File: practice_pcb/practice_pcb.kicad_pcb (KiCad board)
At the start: 2 copper layers, 61.5 x 44 mm, 22 parts, among them J1 VEE connector, J2 From_MCU, J3 MOSFET_out, J4 Conn_01x03, J5 Conn_01x01_Socket, J6 Conn_01x01_Socket, Q4 IRF3710, U1 LDO-3.3, U5 NSi6651A

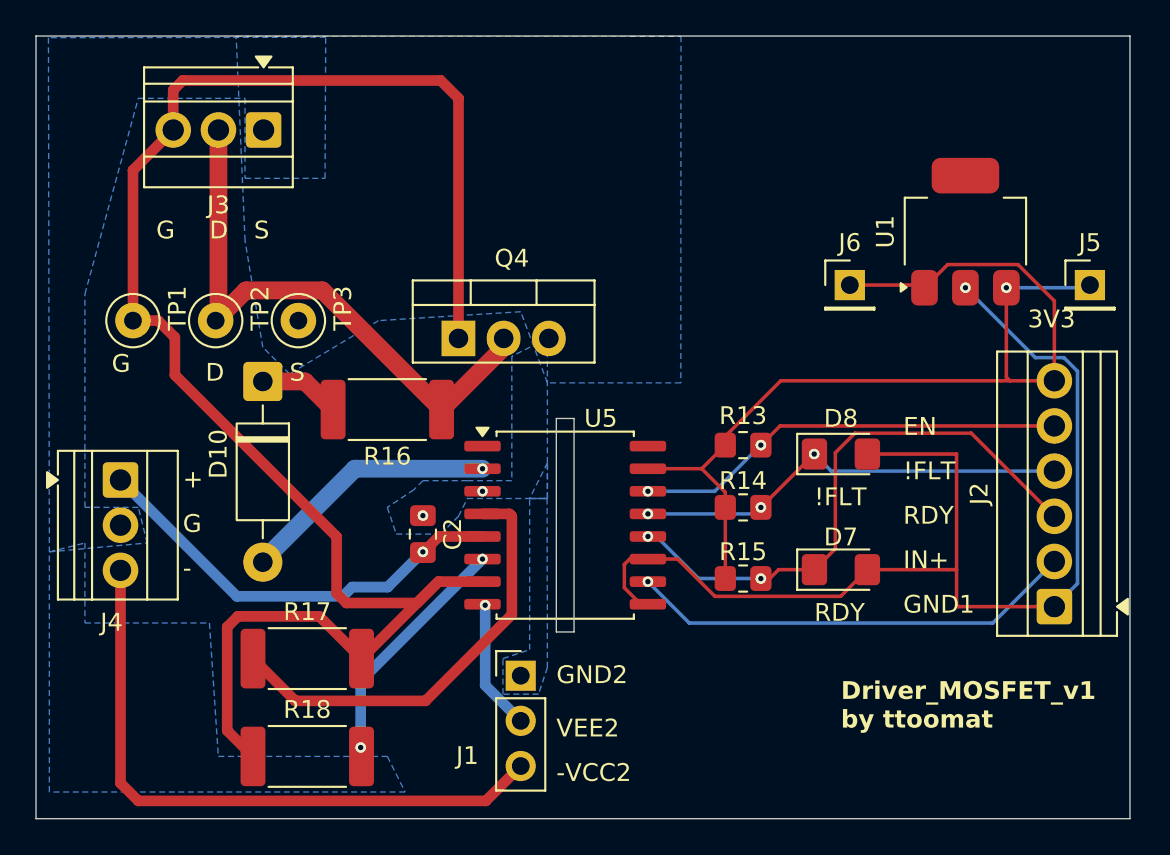
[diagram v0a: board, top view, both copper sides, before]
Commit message: practice_pcb driver schematics changed (leds).
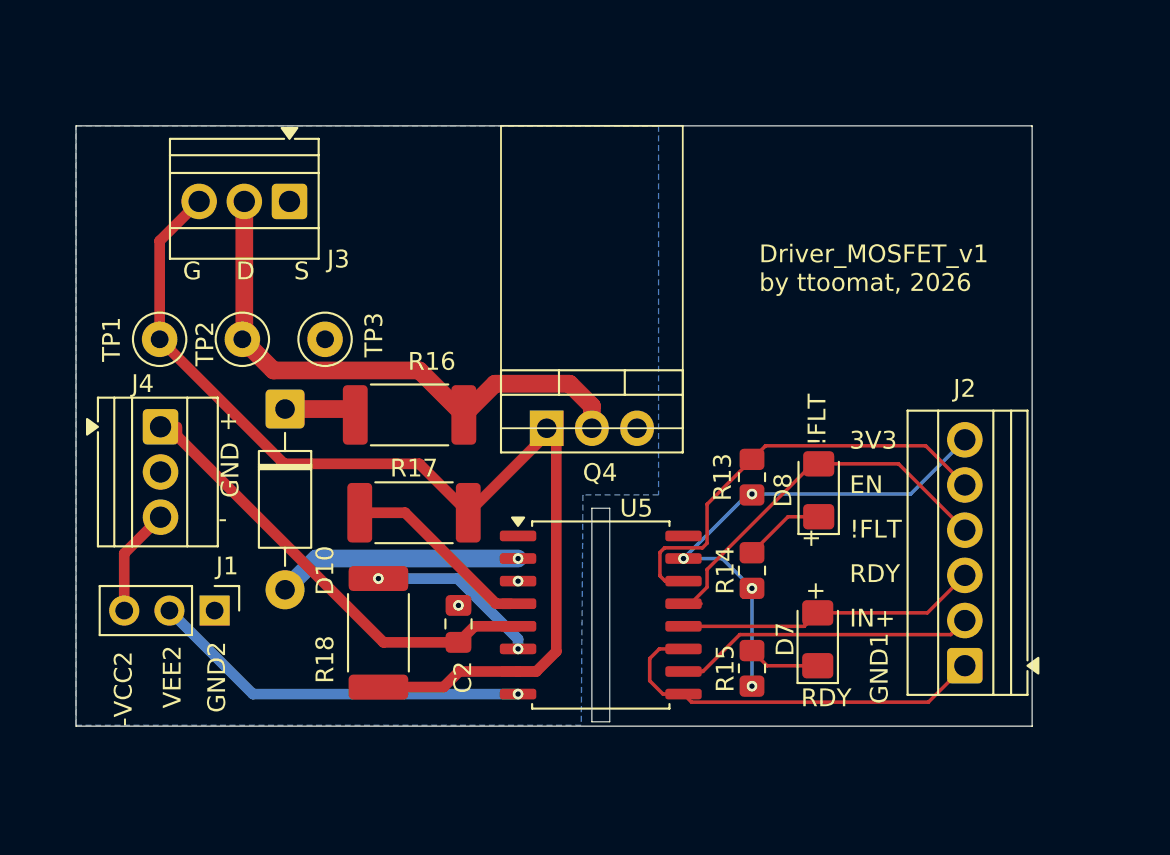
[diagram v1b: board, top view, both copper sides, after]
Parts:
- removed J5, J6: Conn_01x01_Socket, Connector_PinHeader_2.54mm:PinHeader_1x01_P2.54mm_Vertical
- removed U1: LDO-3.3, Package_TO_SOT_SMD:SOT-223-3_TabPin2
- R13, R14, R15: value 4.7k -> 1k
- moved J1 17.6 mm to (93.8, 84.8), turned to -90 degrees
- moved R17 10.2 mm to (105.0, 79.3)
- moved R18 8.02 mm to (103.0, 86.0), turned to 90 degrees
- moved Q4 7.08 mm to (112.5, 74.5)
- moved J2 6.03 mm to (136.0, 87.9)
- moved C2 5.43 mm to (107.5, 85.5)
- moved U5 5.43 mm to (115.5, 85.0)
- moved R15 5.07 mm to (124.0, 88.0), turned to 90 degrees
- moved J3 4.27 mm to (98.0, 61.8)
- moved D7 4.13 mm to (127.7, 86.4), turned to 90 degrees
- moved J4 3.74 mm to (90.8, 74.5)
- moved R14 3.59 mm to (124.0, 82.5), turned to 90 degrees
- moved D8 2.39 mm to (127.8, 78.0), turned to 90 degrees
- moved D10 1.99 mm to (97.8, 73.5)
- moved R13 1.87 mm to (124.0, 77.3), turned to 90 degrees
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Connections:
- D7 pad 2: GND_DRV1 -> Net-(D7-A)
- D8 pad 2: GND_DRV1 -> Net-(D8-A)
- J2 pad 3: Net-(D7-K) -> Net-(D7-A)
- J2 pad 4: Net-(D8-K) -> Net-(D8-A)
- J2 pad 6: Net-(J2-Pin_6) -> +3V3_DRV1
- U5 pad 12: Net-(D7-K) -> Net-(D7-A)
- U5 pad 13: Net-(D8-K) -> Net-(D8-A)
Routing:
- net GND_DRV1: track 64.4 -> 22.8 mm, vias 1 -> 0
- net Net-(J3-Pin_3): track 96.7 -> 61.5 mm
- net -15_DRV2: track 35.7 -> 6.09 mm
- net Net-(D7-K): track 32.3 -> 4.05 mm, vias 2 -> 0
- net Net-(D8-A): track 0.00 -> 22.2 mm
- net Net-(D8-K): track 24.7 -> 4.59 mm, vias 3 -> 0
- net Net-(J2-Pin_6): track 17.0 -> 0.00 mm
- net Net-(D7-A): track 0.00 -> 17.0 mm
- net Net-(J1-Pin_2): track 7.33 -> 21.5 mm
- net Net-(U5-OUTH): track 24.8 -> 11.0 mm
- net +3V3_DRV1: track 42.2 -> 29.6 mm, vias 1 -> 4
- net Net-(J2-Pin_2): track 25.2 -> 17.1 mm, vias 1 -> 0
- net Net-(U5-OUTL): track 13.4 -> 9.81 mm
- net +15_DRV2: track 24.5 -> 25.8 mm, vias 1 -> 0
- net /SINE (from OpAmp): track 32.6 -> 31.7 mm
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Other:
- board size 61.5 x 44 mm -> 53.8 x 33.8 mm
- board text added: "Driver_MOSFET_v1 by ttoomat, 2026"
- board text added: "GND"
- board text removed: "Driver_MOSFET_v1 by ttoomat"

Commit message: Driver board: castellated holes. SMD diode.
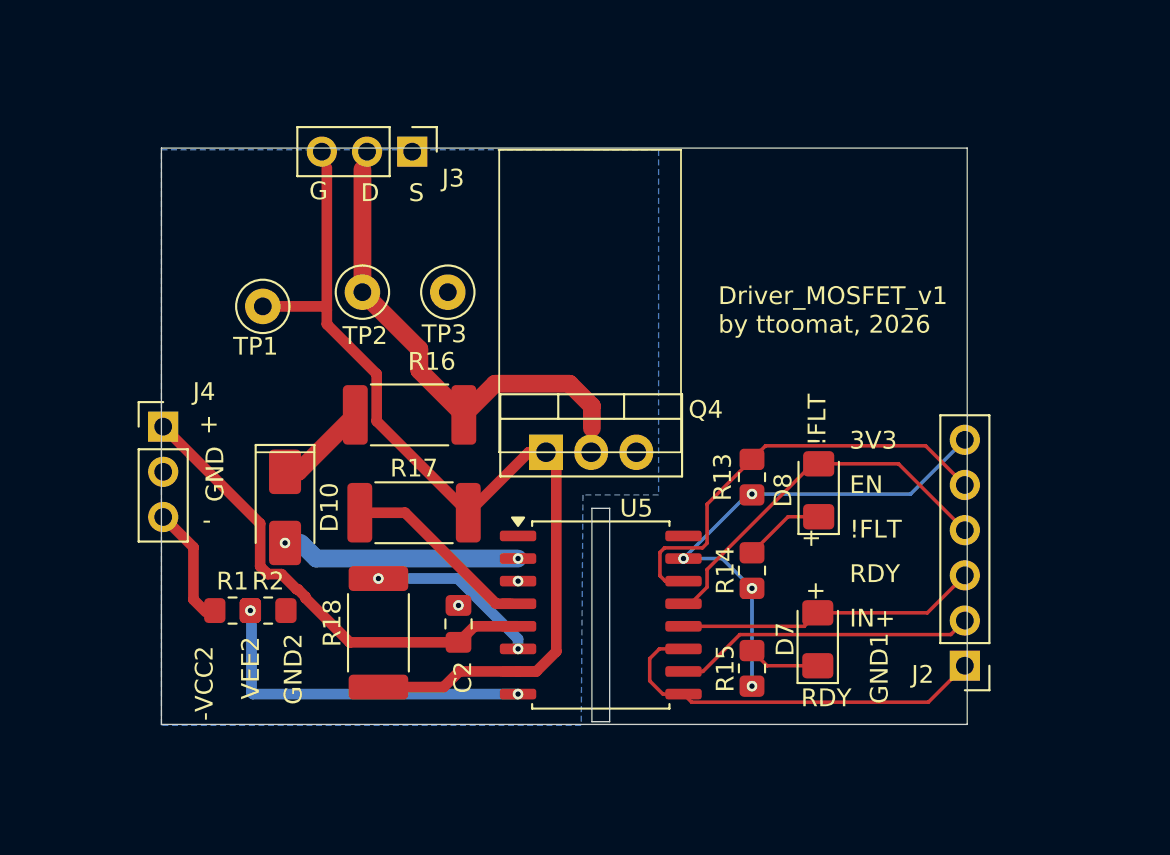
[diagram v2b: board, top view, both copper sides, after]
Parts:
- removed J1: VEE connector, Connector_PinHeader_2.54mm:PinHeader_1x03_P2.54mm_Vertical
- added R1: 0, Resistor_SMD:R_0805_2012Metric_Pad1.20x1.40mm_HandSolder, F.Cu at (94.8, 84.8)
- added R2: 0, Resistor_SMD:R_0805_2012Metric_Pad1.20x1.40mm_HandSolder, F.Cu at (96.8, 84.8)
- D10: value 1N4006 -> S1K-13-F; footprint Diode_THT:D_DO-41_SOD81_P10.16mm_Horizontal -> Diode_SMD:D_SMA
- J2: footprint TerminalBlock:TerminalBlock_Xinya_XY308-2.54-6P_1x06_P2.54mm_Horizontal -> Connector_PinHeader_2.54mm:PinHeader_1x06_P2.54mm_Vertical
- J3, J4: footprint TerminalBlock:TerminalBlock_Xinya_XY308-2.54-3P_1x03_P2.54mm_Horizontal -> Connector_PinHeader_2.54mm:PinHeader_1x03_P2.54mm_Vertical
- moved J3 7.45 mm to (104.9, 59.0), turned to -90 degrees
- moved TP3 7.39 mm to (106.9, 66.9)
- moved TP2 7.25 mm to (102.1, 66.9)
- moved TP1 6.09 mm to (96.5, 67.7)
- moved D10 5.53 mm to (97.8, 79.0)
- moved Q4 1.35 mm to (112.4, 75.9)
- moved J4 0.15 mm to (90.9, 74.5), turned to 0 degrees
- turned J2 to 180 degrees
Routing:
- net Net-(J3-Pin_3): track 61.5 -> 55.2 mm
- net /SINE (from OpAmp): track 31.7 -> 25.9 mm
- net Net-(R1-Pad2): track 21.5 -> 19.5 mm, vias 1 -> 2
- net Net-(D10-K): track 4.09 -> 5.74 mm
- net Net-(D8-A): track 22.2 -> 21.2 mm
- net Net-(D10-A): track 13.8 -> 13.5 mm, vias 1 -> 2
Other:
- board size 53.8 x 33.8 mm -> 45.3 x 32.4 mm

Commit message: Driver PCB leds error fixed.
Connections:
- D7 pad 2: Net-(D7-A) -> GND_DRV1
- D8 pad 2: Net-(D8-A) -> GND_DRV1
- J2 pad 3: Net-(D7-A) -> Net-(D7-K)
- J2 pad 4: Net-(D8-A) -> Net-(D8-K)
- U5 pad 12: Net-(D7-A) -> Net-(D7-K)
- U5 pad 13: Net-(D8-A) -> Net-(D8-K)
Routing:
- net GND_DRV1: track 22.8 -> 52.2 mm
- net Net-(D8-A): track 21.2 -> 0.00 mm
- net Net-(D7-A): track 17.0 -> 0.00 mm
- net Net-(D7-K): track 4.05 -> 18.8 mm, vias 0 -> 1
- net Net-(D8-K): track 4.59 -> 17.7 mm
- net Net-(J2-Pin_2): track 17.1 -> 18.3 mm, vias 0 -> 1
- net Net-(J2-Pin_5): track 25.2 -> 24.6 mm
- net GND_DRV2: vias 2 -> 3
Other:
- board size 45.3 x 32.4 mm -> 45.4 x 32.4 mm

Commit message: Lab consultation.
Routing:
- net /SINE (from OpAmp): track 25.9 -> 28.3 mm
- net Net-(J3-Pin_3): track 55.2 -> 56.2 mm
- net Net-(D10-A): track 13.5 -> 14.3 mm
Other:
- board size 45.4 x 32.4 mm -> 49 x 34.2 mm
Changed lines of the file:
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@@
 	)
 	(gr_rect
-		(start 90.8 58.8)
-		(end 136.2 91.2)
+		(start 89 57)
+		(end 138 91.2)
 		(stroke
 			(width 0.05)
@@
 	)
 	(segment
+		(start 120.855 90.2)
+		(end 120.15 89.495)
+		(width 0.2)
+		(layer "F.Cu")
+		(net "GND_DRV1")
+	)
+	(segment
+		(start 137.1175 86.75)
+		(end 137.1175 79.803654)
+		(width 0.2)
+		(layer "F.Cu")
+		(net "GND_DRV1")
+	)
+	(segment
+		(start 120.545552 86.955)
+		(end 120.15 86.955)
+		(width 0.2)
+		(layer "F.Cu")
+		(net "GND_DRV1")
+	)
+	(segment
+		(start 118.25 87.5)
+		(end 118.25 88.75)
+		(width 0.2)
+		(layer "F.Cu")
+		(net "GND_DRV1")
+	)
+	(segment
+		(start 135.9675 87.9)
+		(end 137.1175 86.75)
+		(width 0.2)
+		(layer "F.Cu")
+		(net "GND_DRV1")
+	)
+	(segment
+		(start 130.325 79.125)
+		(end 127.75 76.55)
+		(width 0.2)
+		(layer "F.Cu")
+		(net "GND_DRV1")
+	)
+	(segment
+		(start 133.6675 90.2)
+		(end 120.855 90.2)
+		(width 0.2)
+		(layer "F.Cu")
+		(net "GND_DRV1")
+	)
+	(segment
+		(start 118.795 86.955)
+		(end 118.25 87.5)
+		(width 0.2)
+		(layer "F.Cu")
+		(net "GND_DRV1")
+	)
+	(segment
+		(start 136.438846 79.125)
+		(end 130.325 79.125)
+		(width 0.2)
+		(layer "F.Cu")
+		(net "GND_DRV1")
+	)
+	(segment
+		(start 118.995 89.495)
+		(end 120.15 89.495)
+		(width 0.2)
+		(layer "F.Cu")
+		(net "GND_DRV1")
+	)
+	(segment
+		(start 137.1175 79.803654)
+		(end 136.438846 79.125)
+		(width 0.2)
+		(layer "F.Cu")
+		(net "GND_DRV1")
+	)
+	(segment
+		(start 127.75 76.55)
+		(end 127.415256 76.55)
+		(width 0.2)
+		(layer "F.Cu")
+		(net "GND_DRV1")
+	)
+	(segment
+		(start 120.15 86.955)
+		(end 118.795 86.955)
+		(width 0.2)
+		(layer "F.Cu")
+		(net "GND_DRV1")
+	)
+	(segment
+		(start 132.995 84.9275)
+		(end 127.697336 84.9275)
+		(width 0.2)
+		(layer "F.Cu")
+		(net "GND_DRV1")
+	)
+	(segment
+		(start 135.9675 87.9)
+		(end 132.995 84.9275)
+		(width 0.2)
+		(layer "F.Cu")
+		(net "GND_DRV1")
+	)
+	(segment
+		(start 135.9675 87.9)
+		(end 133.6675 90.2)
+		(width 0.2)
+		(layer "F.Cu")
+		(net "GND_DRV1")
+	)
+	(segment
+		(start 118.25 88.75)
+		(end 118.995 89.495)
+		(width 0.2)
+		(layer "F.Cu")
+		(net "GND_DRV1")
+	)
+	(segment
 		(start 113.75 72.05)
 		(end 115 73.3)
@@
 	)
 	(segment
+		(start 107.8 73.8)
+		(end 109.55 72.05)
+		(width 1)
+		(layer "F.Cu")
+		(net "/SINE (from OpAmp)")
+	)
+	(segment
+		(start 115 75.86)
+		(end 114.96 75.9)
+		(width 1)
+		(layer "F.Cu")
+		(net "/SINE (from OpAmp)")
+	)
+	(segment
 		(start 105.3 71.3)
 		(end 107.8 73.8)
@@
 	)
 	(segment
-		(start 115 73.3)
-		(end 115 74.55)
-		(width 1)
-		(layer "F.Cu")
-		(net "/SINE (from OpAmp)")
-	)
-	(segment
 		(start 105.3 71.3)
 		(end 105.3 70.1)
@@
 	)
 	(segment
-		(start 107.8 73.8)
-		(end 109.55 72.05)
+		(start 102.1 66.9)
+		(end 102.1 59.26)
+		(width 1)
+		(layer "F.Cu")
+		(net "/SINE (from OpAmp)")
+	)
+	(segment
+		(start 115 73.3)
+		(end 115 75.86)
 		(width 1)
 		(layer "F.Cu")
@@
 	)
 	(segment
-		(start 102.1 66.9)
-		(end 102.1 60)
+		(start 102.1 59.26)
+		(end 102.36 59)
 		(width 1)
 		(layer "F.Cu")
@@
 	)
 	(segment
+		(start 99.82 59)
+		(end 100.1 59.28)
+		(width 0.6)
+		(layer "F.Cu")
+		(net "Net-(J3-Pin_3)")
+	)
+	(segment
 		(start 106.665256 89.1)
 		(end 103 89.1)
@@
 	)
 	(segment
+		(start 100.1 59.28)
+		(end 100.1 67.9)
+		(width 0.6)
+		(layer "F.Cu")
+		(net "Net-(J3-Pin_3)")
+	)
+	(segment
 		(start 102.9 74.15)
 		(end 108.05 79.3)
@@
 	)
 	(segment
-		(start 100.1 59.9)
-		(end 100.1 67.9)
-		(width 0.6)
-		(layer "F.Cu")
-		(net "Net-(J3-Pin_3)")
-	)
-	(segment
 		(start 113 76.48)
 		(end 113 87.099999)
@@
 	)
 	(segment
-		(start 98.63 81)
-		(end 99.505 81.875)
+		(start 99.63 80)
+		(end 98.63 81)
 		(width 1)
 		(layer "B.Cu")
@@
 	)
 	(segment
+		(start 108.975 80)
+		(end 99.63 80)
+		(width 1)
+		(layer "B.Cu")
+		(net "Net-(D10-A)")
+	)
+	(segment
 		(start 110.85 81.875)
-		(end 99.505 81.875)
+		(end 108.975 80)
 		(width 1)
 		(layer "B.Cu")
@@
 	)
 	(segment
-		(start 103 83)
-		(end 107.45 83)
+		(start 109.95 85.5)
+		(end 110.85 86.4)
+		(width 0.6)
+		(layer "B.Cu")
+		(net "Net-(U5-OUTL)")
+	)
+	(segment
+		(start 105.5 85.5)
+		(end 109.95 85.5)
 		(width 0.6)
 		(layer "B.Cu")
@@
 	)
 	(segment
-		(start 107.45 83)
-		(end 110.85 86.4)
+		(start 103 83)
+		(end 105.5 85.5)
 		(width 0.6)
 		(layer "B.Cu")
 		(net "Net-(U5-OUTL)")
-	)
-	(segment
-		(start 120.855 90.2)
-		(end 120.15 89.495)
-		(width 0.2)
-		(layer "F.Cu")
-		(net "GND_DRV1")
-	)
-	(segment
-		(start 137.1175 86.75)
-		(end 137.1175 79.803654)
-		(width 0.2)
-		(layer "F.Cu")
-		(net "GND_DRV1")
-	)
-	(segment
-		(start 120.545552 86.955)
-		(end 120.15 86.955)
-		(width 0.2)
-		(layer "F.Cu")
-		(net "GND_DRV1")
-	)
-	(segment
-		(start 118.25 87.5)
-		(end 118.25 88.75)
-		(width 0.2)
-		(layer "F.Cu")
-		(net "GND_DRV1")
-	)
-	(segment
-		(start 135.9675 87.9)
-		(end 137.1175 86.75)
-		(width 0.2)
-		(layer "F.Cu")
-		(net "GND_DRV1")
-	)
-	(segment
-		(start 130.325 79.125)
-		(end 127.75 76.55)
-		(width 0.2)
-		(layer "F.Cu")
-		(net "GND_DRV1")
-	)
-	(segment
-		(start 133.6675 90.2)
-		(end 120.855 90.2)
-		(width 0.2)
-		(layer "F.Cu")
-		(net "GND_DRV1")
-	)
-	(segment
-		(start 118.795 86.955)
-		(end 118.25 87.5)
-		(width 0.2)
-		(layer "F.Cu")
-		(net "GND_DRV1")
-	)
-	(segment
-		(start 136.438846 79.125)
-		(end 130.325 79.125)
-		(width 0.2)
-		(layer "F.Cu")
-		(net "GND_DRV1")
-	)
-	(segment
-		(start 118.995 89.495)
-		(end 120.15 89.495)
-		(width 0.2)
-		(layer "F.Cu")
-		(net "GND_DRV1")
-	)
-	(segment
-		(start 137.1175 79.803654)
-		(end 136.438846 79.125)
-		(width 0.2)
-		(layer "F.Cu")
-		(net "GND_DRV1")
-	)
-	(segment
-		(start 127.75 76.55)
-		(end 127.415256 76.55)
-		(width 0.2)
-		(layer "F.Cu")
-		(net "GND_DRV1")
-	)
-	(segment
-		(start 120.15 86.955)
-		(end 118.795 86.955)
-		(width 0.2)
-		(layer "F.Cu")
-		(net "GND_DRV1")
-	)
-	(segment
-		(start 132.995 84.9275)
-		(end 127.697336 84.9275)
-		(width 0.2)
-		(layer "F.Cu")
-		(net "GND_DRV1")
-	)
-	(segment
-		(start 135.9675 87.9)
-		(end 132.995 84.9275)
-		(width 0.2)
-		(layer "F.Cu")
-		(net "GND_DRV1")
-	)
-	(segment
-		(start 135.9675 87.9)
-		(end 133.6675 90.2)
-		(width 0.2)
-		(layer "F.Cu")
-		(net "GND_DRV1")
-	)
-	(segment
-		(start 118.25 88.75)
-		(end 118.995 89.495)
-		(width 0.2)
-		(layer "F.Cu")
-		(net "GND_DRV1")
 	)
 	(segment
@@
 		(polygon
 			(pts
-				(xy 90.8 58.9) (xy 118.75 58.9) (xy 118.75 78.3) (xy 114.5 78.3) (xy 114.4 91.25) (xy 90.8 91.25)
-			)
-		)
+				(xy 89 57) (xy 118.75 57) (xy 118.75 77.5) (xy 114.5 77.5) (xy 114.4 91.25) (xy 89 91.25)
+			)
+		)

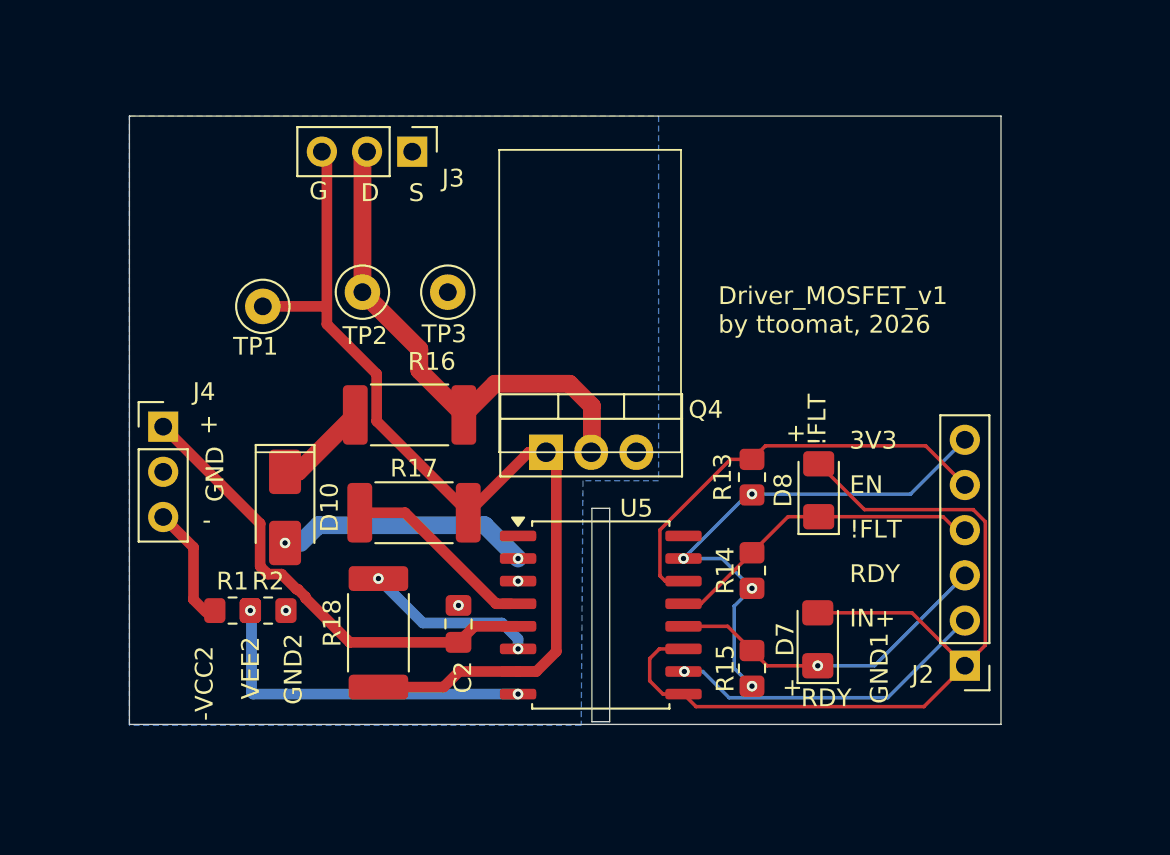
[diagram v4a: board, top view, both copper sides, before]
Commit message: Drivers: LEDs deleted + polygon 3.3V added.
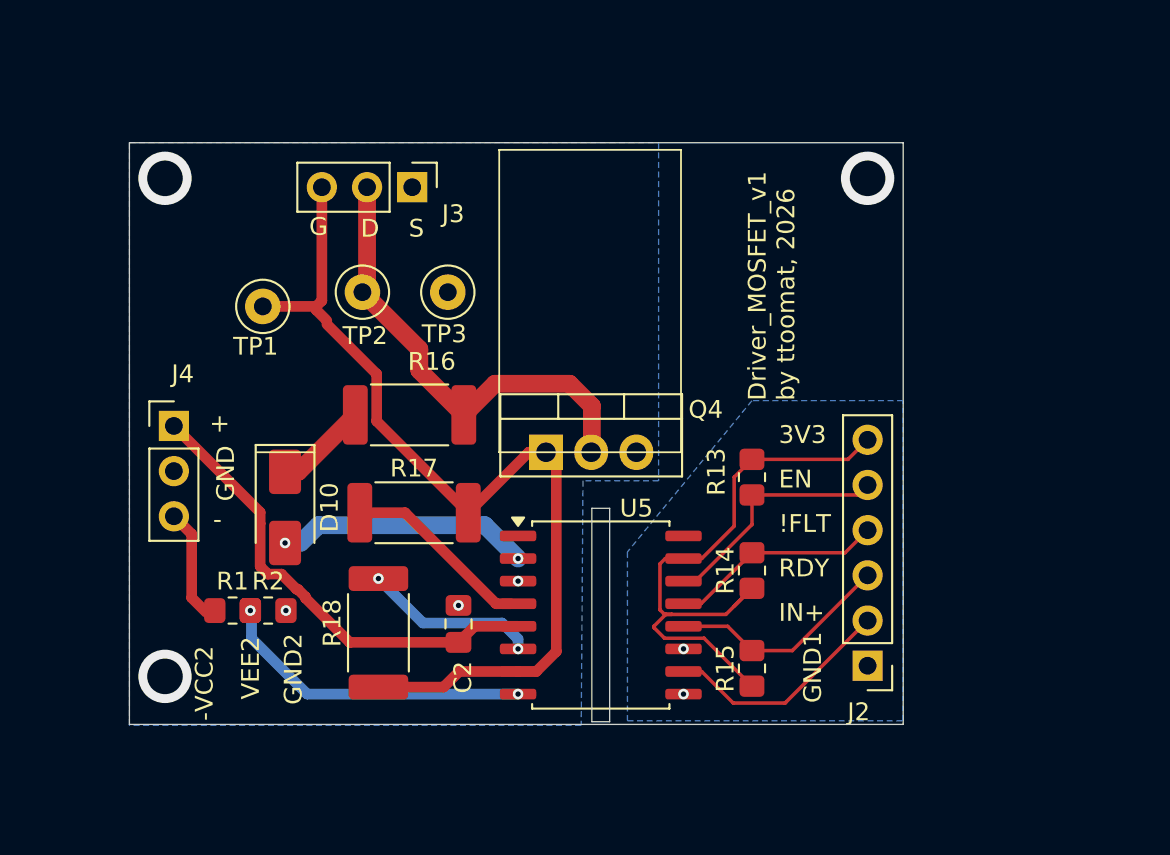
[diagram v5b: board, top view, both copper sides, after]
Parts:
- removed D7, D8: Green LED, LED_SMD:LED_1206_3216Metric_Pad1.42x1.75mm_HandSolder
- moved J2 5.47 mm to (130.5, 87.9)
- moved J3 2.00 mm to (104.9, 61.0)
- moved J4 0.60 mm to (91.5, 74.4)
- turned R13 to -90 degrees
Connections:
- net /SINE (from OpAmp) renamed drain
- net GND_DRV2 renamed source
- net Net-(J3-Pin_3) renamed gate
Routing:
- net GND_DRV1: track 52.2 -> 0.40 mm, vias 0 -> 2
- net Net-(J2-Pin_5): track 24.6 -> 13.6 mm
- net Net-(J2-Pin_3): track 18.8 -> 12.7 mm, vias 1 -> 0
- net Net-(J2-Pin_4): track 17.7 -> 12.1 mm
- net Net-(J2-Pin_2): track 18.3 -> 13.2 mm, vias 1 -> 0
- net +3V3_DRV1: track 29.6 -> 34.3 mm, vias 4 -> 0
- net gate: track 56.2 -> 53.6 mm
- net drain: track 28.3 -> 26.3 mm
- net Net-(R1-Pad2): track 19.5 -> 17.7 mm
- net source: vias 3 -> 5
- net (no net): vias 0 -> 1
- added copper zone on B.Cu, net GND_DRV1
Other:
- board size 49 x 34.2 mm -> 43.5 x 32.7 mm
